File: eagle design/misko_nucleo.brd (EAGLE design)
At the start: 115 x 73 mm, 91 parts, among them CN1 LiPo Battery, IC1 TPS63031, IC1101 47309-2651, IC1201 FM25W256, IC1301 ADXL345, IC1302 74HCT1G32GW, IC2 RN4678_BT_MODULE, IC3 MAX6818, Q1 BSS84, Q1701 SQ2310ES-T1_BE3, Q1702 SQ2310ES-T1_BE3, Q1703 SQ2310ES-T1_BE3, SW1 MICROJOYSTICK, SW2 PB6156RSL, SW3 PB6156RSL, U1 SN74LVC1G3157DBVR - BT switch, U2 ATMEGA1281-16AU, U3 MCP73871-2AAI/ML, U4 SN74LVC1G3157DBVR - GPS switch, X1 FH12-30S-0.5SH

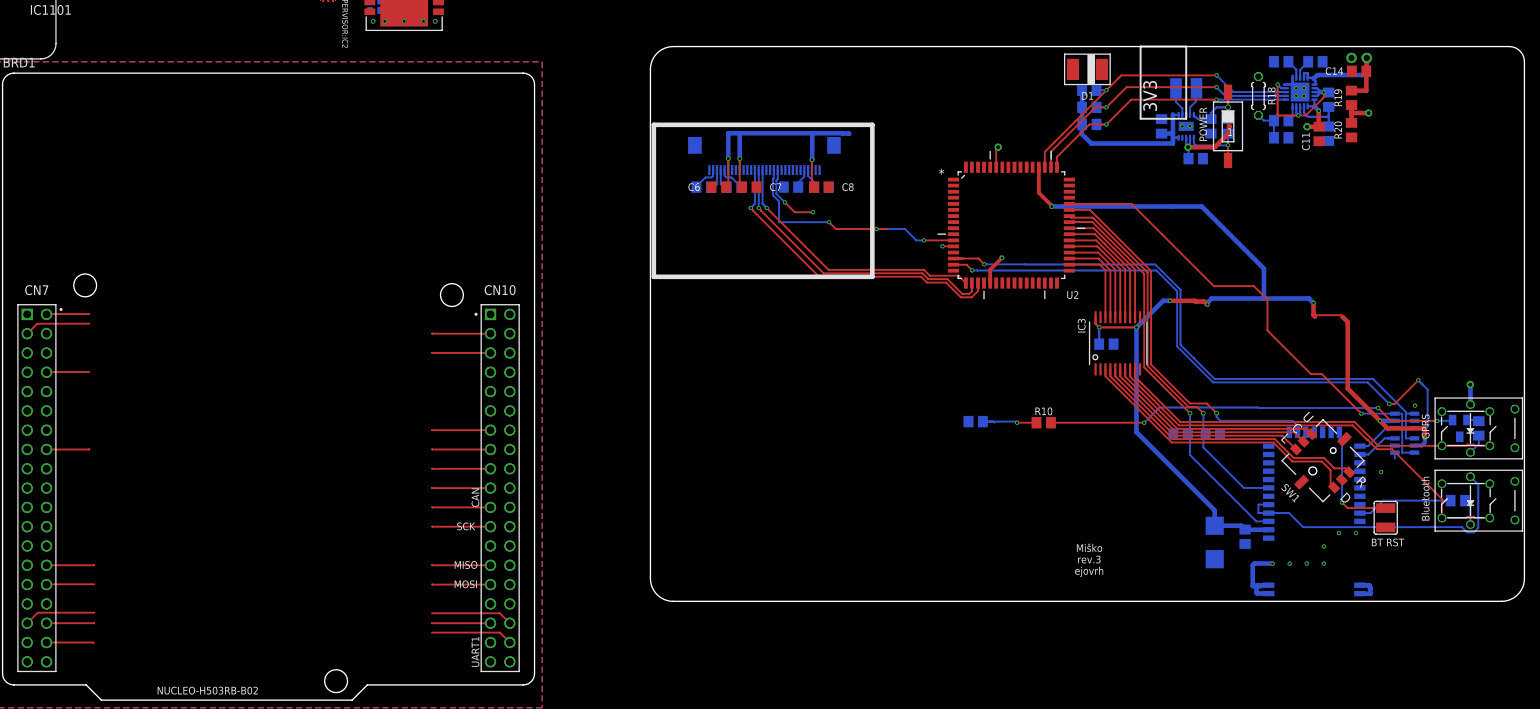
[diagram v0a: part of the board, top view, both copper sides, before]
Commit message: in misko.ioc: - moved SPI1_SD_CS from PA1 to PA2 - added timer2 rotary encoder GPIOs on PA1 and PB2 - added I2C2 in DMA mode
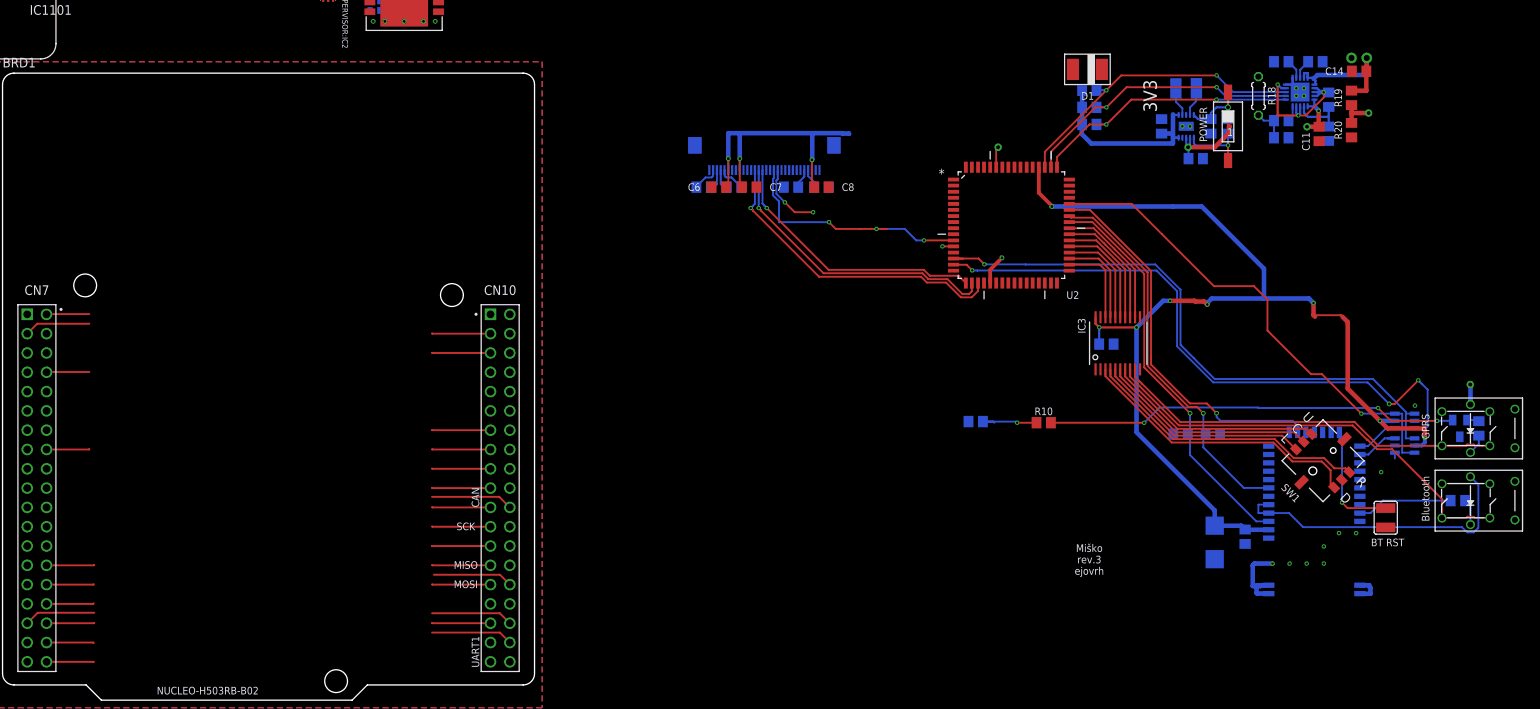
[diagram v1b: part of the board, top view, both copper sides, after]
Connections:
- net PB10 renamed I2C2_SCL
- net PB13 renamed I2C2_SDA
- net PB2 renamed ROTARY_CH1
- removed net PA2: BRD1.CN7_32
- new net ROTARY_CH2: BRD1.CN7_30
- net SPI1_SD_CS: now also BRD1.CN7_32; no longer BRD1.CN7_30
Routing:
- net ROTARY_CH1: track 0.00 -> 10.8 mm
- net I2C2_SDA: track 0.00 -> 10.5 mm
- net I2C2_SCL: track 0.00 -> 7.72 mm
- net ROTARY_CH2: track 0.00 -> 6.23 mm
- net LED_YELLOW: track 0.00 -> 6.23 mm
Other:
- board size 115 x 73 mm -> 70 x 82.5 mm
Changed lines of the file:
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@@
 <board>
 <plain>
-<wire x1="88.25" y1="13" x2="197.25" y2="13" width="0.1" layer="20"/>
-<wire x1="200.25" y1="16" x2="200.25" y2="84" width="0.1" layer="20"/>
-<wire x1="198.25" y1="86" x2="88.25" y2="86" width="0.1" layer="20"/>
-<wire x1="85.25" y1="83" x2="85.25" y2="16" width="0.1" layer="20"/>
-<wire x1="85.25" y1="83" x2="88.25" y2="86" width="0.1" layer="20" curve="-90"/>
-<wire x1="85.25" y1="16" x2="88.25" y2="13" width="0.1" layer="20" curve="90"/>
-<wire x1="197.25" y1="13" x2="200.25" y2="16" width="0.1" layer="20" curve="90"/>
-<wire x1="198.25" y1="86" x2="200.25" y2="84" width="0.1" layer="20" curve="-90"/>
-<wire x1="168" y1="78.25" x2="149.2" y2="78.15" width="0.5" layer="22" style="shortdash"/>
 <wire x1="156" y1="72.75" x2="154.5" y2="72.75" width="0.5" layer="22" style="shortdash"/>
-<wire x1="131" y1="72.75" x2="149.2" y2="72.65" width="0.5" layer="22" style="shortdash"/>
-<wire x1="149.2" y1="72.65" x2="149.2" y2="78.15" width="0.5" layer="22" style="shortdash"/>
-<wire x1="114.45" y1="55.7" x2="114.45" y2="75.7" width="0.6" layer="21"/>
-<wire x1="85.7" y1="55.7" x2="85.7" y2="75.7" width="0.6" layer="21"/>
-<wire x1="85.7" y1="55.7" x2="114.45" y2="55.7" width="0.6" layer="21"/>
-<wire x1="85.7" y1="75.7" x2="114.45" y2="75.7" width="0.6" layer="21"/>
 <text x="151" y="79.5" size="1.778" layer="21" font="vector" rot="R90" align="center">3V3</text>
 <text x="158" y="75.75" size="1" layer="21" font="vector" rot="R270" align="center">POWER</text>
@@
 <wire x1="179.75" y1="77.25" x2="168" y2="77.25" width="0.5" layer="22" style="shortdash"/>
 <text x="182.25" y="20.75" size="1" layer="21" font="vector" align="center">BT RST</text>
-<wire x1="171.75" y1="75.25" x2="171.75" y2="41.5" width="0.5" layer="22" style="shortdash"/>
-<wire x1="171.75" y1="41.5" x2="193.25" y2="41.5" width="0.5" layer="22" style="shortdash"/>
-<wire x1="149.75" y1="86" x2="155.75" y2="86" width="0.25" layer="21"/>
-<wire x1="155.75" y1="86" x2="155.75" y2="76.5" width="0.25" layer="21"/>
-<wire x1="155.75" y1="76.5" x2="149.75" y2="76.5" width="0.25" layer="21"/>
-<wire x1="149.75" y1="76.5" x2="149.75" y2="86" width="0.25" layer="21"/>
 <text x="143" y="16.5" size="1" layer="21" align="bottom-center">Miško
 rev.3
@@
 <contactref element="BRD1" pad="CN7_38"/>
 <contactref element="Q1703" pad="1"/>
-<wire x1="5.79" y1="5.04" x2="18.55" y2="-7.65" width="0" layer="19" extent="16-16"/>
+<wire x1="5.79" y1="5.04" x2="11.96" y2="5.04" width="0.25" layer="1"/>
+<wire x1="11.96" y1="5.04" x2="12" y2="5" width="0.25" layer="1"/>
+<wire x1="12" y1="5" x2="18.55" y2="-7.65" width="0" layer="19" extent="1-16"/>
 </signal>
 <signal name="PA15" class="2">
@@
 </signal>
 <signal name="SPI1_SD_CS" class="2">
-<contactref element="BRD1" pad="CN7_30"/>
-<wire x1="5.79" y1="15.2" x2="5.83" y2="15.24" width="0.25" layer="1"/>
-<wire x1="5.83" y1="15.24" x2="12.065" y2="15.24" width="0.25" layer="1"/>
 <contactref element="IC1101" pad="CD/DAT3"/>
-<wire x1="5.79" y1="15.2" x2="3.78" y2="97.74" width="0" layer="19" extent="1-1"/>
+<contactref element="BRD1" pad="CN7_32"/>
+<wire x1="5.79" y1="12.66" x2="11.91" y2="12.66" width="0.25" layer="1"/>
+<wire x1="11.91" y1="12.66" x2="12" y2="12.75" width="0.25" layer="1"/>
+<wire x1="5.79" y1="12.66" x2="3.78" y2="97.74" width="0" layer="19" extent="1-1"/>
 </signal>
 <signal name="ADC_VGPS" class="2">
@@
 <contactref element="BRD1" pad="CN10_24"/>
 </signal>
-<signal name="PB2" class="2">
+<signal name="ROTARY_CH1" class="2">
 <contactref element="BRD1" pad="CN10_22"/>
+<wire x1="66.75" y1="25.36" x2="65.36" y2="26.75" width="0.25" layer="1"/>
+<wire x1="65.36" y1="26.75" x2="56.5" y2="26.75" width="0.25" layer="1"/>
 </signal>
 <signal name="SPI1_MISO" class="2">
@@
 <wire x1="65.44" y1="8.89" x2="56.515" y2="8.89" width="0.25" layer="1"/>
 </signal>
-<signal name="PB10" class="2">
+<signal name="I2C2_SCL" class="2">
 <contactref element="BRD1" pad="CN10_25"/>
+<wire x1="64.21" y1="20.28" x2="56.53" y2="20.28" width="0.25" layer="1"/>
+<wire x1="56.53" y1="20.28" x2="56.5" y2="20.25" width="0.25" layer="1"/>
 </signal>
 <signal name="PN12" class="2">
 <contactref element="BRD1" pad="CN10_16"/>
 </signal>
-<signal name="PB13" class="2">
+<signal name="I2C2_SDA" class="2">
 <contactref element="BRD1" pad="CN10_30"/>
+<wire x1="66.75" y1="15.2" x2="65.45" y2="16.5" width="0.25" layer="1"/>
+<wire x1="65.45" y1="16.5" x2="56.75" y2="16.5" width="0.25" layer="1"/>
 </signal>
 <signal name="5V0" class="3">
@@
 <signal name="ADXL345:ADXL345_INT2">
 <contactref element="IC1301" pad="INT2"/>
-</signal>
-<signal name="PA2" class="2">
-<contactref element="BRD1" pad="CN7_32"/>
 </signal>
 <signal name="GPS:SUPERCAP+CHARGER:VMID" class="2">
@@
 <wire x1="5.79" y1="7.58" x2="-18.65" y2="77.2" width="0" layer="19" extent="16-16"/>
 </signal>
+<signal name="ROTARY_CH2" class="2">
+<contactref element="BRD1" pad="CN7_30"/>
+<wire x1="5.79" y1="15.2" x2="11.95" y2="15.2" width="0.25" layer="1"/>
+<wire x1="11.95" y1="15.2" x2="12" y2="15.25" width="0.25" layer="1"/>
+</signal>
 </signals>

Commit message: in sch & brd: - changed hierarchical module names so that board components have shorter names (GPS subsystem stuff) - added CAN infra. components to sch
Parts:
- removed C1, C10, C13, C8: 10µF, rcl:C0805
- removed C11, C14: 10µF, resistor:C0805
- removed C12: 1000µF, rcl:E5-10,5
- removed C2: 0.1µF, rcl:C0805
- removed C3, C4, C6, C7: 1µF, rcl:C0805
- removed C5: 22µF, rcl:C0805
- removed C9: 2.2µF / 25V, rcl:C0805
- removed CN1: LiPo Battery, SIM800C:JST-PH-2-THM-RA
- removed D1: BZG05C3V6-E3-TR3, zener:DO-214
- removed D2: SZ1SMB5916BT3G, diode:SMB
- removed D3: BAT60AE6327, diode:SOD323_ST
- removed GPS:ORG1510:IC1: ORG1510-MK4, ORG1510-MK4 GPS module:SMD
- removed GPS:SUPERCAP+CHARGER:C1, GPS:SUPERCAP+CHARGER:C34: 100u / 16V, rcl:C1210
- removed GPS:SUPERCAP+CHARGER:C24: 1.5F, EECS5R5H155 Supercap:TH
- removed GPS:SUPERCAP+CHARGER:C38, GPS:VOLTAGE_SUPERVISOR:C1, GPS:VOLTAGE_SUPERVISOR:C2: 0.1u / 16V, rcl:C0402
- removed GPS:SUPERCAP+CHARGER:IC2: LTC4425EDD#PBF, LTC4425 Supercap Charger:DFN-12
- removed GPS:SUPERCAP+CHARGER:R1: 33R, resistor:R1206
- removed GPS:SUPERCAP+CHARGER:R14: 10k, resistor:R0402
- removed GPS:SUPERCAP+CHARGER:R40, GPS:SUPERCAP+CHARGER:R41: 150k, resistor:R0402
- removed GPS:VOLTAGE_SUPERVISOR:IC2: TPS3808G33DBVT, TPS3808 - Supervisory Circuit:WSON-6
- removed GPS:VOLTAGE_SUPERVISOR:R18: 100k, resistor:R0402
- removed IC1: TPS63031, TPS63031 - Buck Boost Voltage Regulator:SMT
- removed IC2: RN4678_BT_MODULE, RN4678 Bluetooth 4.2 Dual Mode:SMT
- removed IC3: MAX6818, MAX6818 CMOS Switch debouncer:TSSOP20
- removed L1: DJNR3015-1R5, DJNR3015-1R5 Inductor:FFF
- removed Q1: BSS84, transistor-small-signal:SOT23
- removed R1, R10, R12, R13, R9: 10k, resistor:R0805
- removed R11, R6: 1k, resistor:R0805
- removed R14, R15: 1k, rcl:R0805
- removed R16, R2: 100k, rcl:R0805
- removed R17, R3: 270k, rcl:R0805
- removed R18: NTC 10k, rcl:0204/5
- removed R19, R20: 150k, rcl:R0805
- removed R4, R5, R7: 47k, rcl:R0805
- removed R8: 390k, rcl:R0805
- removed S1: POWER SWITCH, smd-special:SMS-001
- removed SJ1: RESET, jumper:SJW
- removed SW1: MICROJOYSTICK, micro joystick:MICROJOYSTICK
- removed SW2, SW3: PB6156RSL, PB6156RSL Illuminated Tact SPST-NO switch:TH
- removed U1: SN74LVC1G3157DBVR - BT switch, Texas Instruments_By_element14_Batch_1:SOT95P280X145-6N
- removed U2: ATMEGA1281-16AU, Atmel_By_element14_Batch_1-00:QFP80P1600X1600X120-64N
- removed U3: MCP73871-2AAI/ML, MCP73871 - Powerpath and Charge Controller:QFN50P400X400X100-21N
- removed U4: SN74LVC1G3157DBVR - GPS switch, Texas Instruments_By_element14_Batch_1:SOT95P280X145-6N
- removed X1: FH12-30S-0.5SH, con-hirose:FH12-30S-0.5SH
- added C401: 47nF / 10V, rcl:C0402
- added C405: 0.1uF / 10V, rcl:C0402
- added GPS:G:IC1: ORG1510-MK4, ORG1510-MK4 GPS module:SMD
- added GPS:SC:C1, GPS:SC:C34: 100u / 16V, rcl:C1210
- added GPS:SC:C24: 1.5F, EECS5R5H155 Supercap:TH
- added GPS:SC:C38, GPS:SV:C1, GPS:SV:C2: 0.1u / 16V, rcl:C0402
- added GPS:SC:IC2: LTC4425EDD#PBF, LTC4425 Supercap Charger:DFN-12
- added GPS:SC:R1: 33R, resistor:R1206
- added GPS:SC:R14: 10k, resistor:R0402
- added GPS:SC:R40, GPS:SC:R41: 150k, resistor:R0402
- added GPS:SV:IC2: TPS3808G33DBVT, TPS3808 - Supervisory Circuit:WSON-6
- added GPS:SV:R18: 100k, resistor:R0402
- added IC401: TCAN334, TCAN33x - 3.3V CAN Transciever:SOT23-8
- added J1: CAN, con-amp:10X02MTA
- added R401, R405: 60, rcl:R0805
- moved C1201 0.25 mm to (24.5, 96.5)
- moved IC1301 0.15 mm to (29.8, 96.5)
- moved C1131 0.15 mm to (0.25, 95.2)
- moved IC1302 0.11 mm to (29.5, 96.5)
- moved C1304 0.11 mm to (32.2, 95.2)
- moved IC1201 0.10 mm to (21.2, 96.5)
- moved IC1101 0.08 mm to (1.00, 99.0)
- renumbered GPS:ORG1510:C1 to GPS:G:C1, GPS:ORG1510:C2 to GPS:G:C2, GPS:ORG1510:C22 to GPS:G:C22, GPS:ORG1510:C31 to GPS:G:C31, GPS:ORG1510:R1 to GPS:G:R1, GPS:ORG1510:R2 to GPS:G:R2, GPS:SUPERCAP+CHARGER:Q4 to GPS:SC:Q4
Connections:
- removed net ADXL345_INT1_INTERRUPT_PIN: U2.25
- removed net ANALOG_SW_CTRL_PIN: U1.6, U2.44, U4.6
- removed net AREF: U2.62
- removed net AVCC: U2.64
- removed net BAT_A_PIN: R19.2, R20.1, U2.59
- removed net BLUETOOTH_PROF_IND_PIN: IC2.P0_5, U2.43
- removed net BLUETOOTH_RX: IC2.RXD, U1.4
- removed net BLUETOOTH_SWITCH_PIN: IC2.SW_BTN, R13.2, U2.41
- removed net BLUETOOTH_TX: IC2.TXD, U4.3
- removed net BLUETOOTH_WAKEUP_PIN: IC2.WAKEUP, R12.2, U2.42
- removed net BT_LED: IC2.LED, R6.1
- removed net BUTTON_BLUETOOTH: IC3.IN7, SW3.3, SW3.4
- removed net BUTTON_CENTER: IC3.IN5, SW1.CENTER
- removed net BUTTON_DOWN: IC3.IN2, SW1.DOWN
- removed net BUTTON_GPRS: IC3.IN8, SW2.3, SW2.4
- removed net BUTTON_LEFT: IC3.IN4, SW1.LEFT
- removed net BUTTON_RIGHT: IC3.IN3, SW1.RIGHT
- removed net BUTTON_UP: IC3.IN6, SW1.UP
- removed net CAP1N: C3.1, X1.5
- removed net CAP1P: C3.2, X1.4
- removed net CAP2N: C4.1, X1.3
- removed net CAP2P: C4.2, X1.2
- removed net EN: IC1.6_EN, R1.2, S1.1
- removed net GPRS_NETLIGHT: R10.1, R9.1
- removed net GPRS_NETLIGHT_GATE: Q1.1, R10.2
- removed net GPS:ORG1510:GPS_RX: GPS:G:C31.1, GPS:G:R2.2, GPS:ORG1510:IC1.RX_10
- removed net GPS:ORG1510:GPS_TX: GPS:G:C22.1, GPS:G:R1.2, GPS:ORG1510:IC1.3_TX
- removed net GPS:SUPERCAP+CHARGER:N$1: GPS:SC:Q4.3, GPS:SUPERCAP+CHARGER:R1.1
- removed net GPS:SUPERCAP+CHARGER:PFI: GPS:SUPERCAP+CHARGER:IC2.PFI, GPS:SUPERCAP+CHARGER:R40.1, GPS:SUPERCAP+CHARGER:R41.2
- removed net GPS:SUPERCAP+CHARGER:PFI_RET: GPS:SUPERCAP+CHARGER:IC2.PFI_RET, GPS:SUPERCAP+CHARGER:R41.1
- removed net GPS:SUPERCAP+CHARGER:PROG: GPS:SUPERCAP+CHARGER:IC2.PROG, GPS:SUPERCAP+CHARGER:R14.2
- removed net GPS:SUPERCAP+CHARGER:VMID: GPS:SUPERCAP+CHARGER:C1.1, GPS:SUPERCAP+CHARGER:C34.2, GPS:SUPERCAP+CHARGER:IC2.VMID
- removed net GPS:VOLTAGE_SUPERVISOR:CT: GPS:VOLTAGE_SUPERVISOR:IC2.CT
- removed net GPS:VOLTAGE_SUPERVISOR:SENSE: GPS:VOLTAGE_SUPERVISOR:C1.1, GPS:VOLTAGE_SUPERVISOR:IC2.SENSE
- removed net GPS_GREEN_LED_PIN: U2.48
- removed net GPS_POWER_CTL_PIN: U2.45
- removed net GPS_RED_LED_PIN: U2.47
- removed net GPS_SW_SERIAL_RX: U1.1, U2.14, U4.4
- removed net GPS_WAKEUP_PIN: U2.46
- removed net IREF: R8.2, X1.26
- removed net JTAG_TCL_PIN: U2.57
- removed net JTAG_TDI_PIN: U2.54
- removed net JTAG_TDO_PIN: U2.55
- removed net JTAG_TMS_PIN: U2.56
- removed net L2: R6.2, SW3.L2
- removed net LDO18_O: IC2.LDO18_O
- removed net LDO33_O: IC2.LDO33_O, IC2.VDD_IO, SW3.L1
- removed net L_L1: IC1.4_L1, L1.P$1
- removed net L_L2: IC1.2_L2, L1.P$2
- removed net MCP73871_CHARGE_STATUS_1_PIN: R7.2, U2.51, U3.8_STAT1
- removed net MCP73871_CHARGE_STATUS_2_PIN: R5.2, U2.50, U3.7_STAT2
- removed net MCP73871_POWER_GOOD_PIN: R4.2, U2.49, U3.!6_PG!
- removed net MENU_BLUETOOTH_POWER_BUTTON_PIN: IC3.OUT7, U2.39
- removed net MENU_CENTER_BUTTON_PIN: IC3.OUT5, U2.37
- removed net MENU_DOWN_BUTTON_PIN: IC3.OUT2, U2.34
- removed net MENU_GPRS_POWER_BUTTON_PIN: IC3.OUT8, U2.40
- removed net MENU_LEFT_BUTTON_PIN: IC3.OUT4, U2.36
- removed net MENU_RIGHT_BUTTON_PIN: IC3.OUT3, U2.35
- removed net MENU_UP_BUTTON_PIN: IC3.OUT6, U2.38
- removed net N$1: R11.1, SW2.L2
- removed net N$11: IC2.!RST_N!, SJ1.1
- removed net N$19: R14.2, R17.1, R18.1
- removed net N$3: Q1.2, R11.2
- removed net N$6: C12.+, D3.C
- removed net OLD_5V0: D3.A, R2.1, U3.17_CE, U3.18_IN1, U3.19_IN2, U3.3_SEL, U3.4_PROG2, U3.9_!TE!
- removed net PDI_UART0_CTS_PIN: U2.1
- removed net PDI_UART0_RX_PIN: U2.2
- removed net PDI_UART0_TX_PIN: U2.3
- removed net PN12: BRD1.CN10_16
- removed net PROG1: R15.1, U3.13_PROG1
- removed net PROG3: R16.1, U3.12_PROG3
- removed net RESET: U2.20
- removed net RTC_INT_INTERRUPT_PIN: U2.26
- removed net SD_CARD_DETECT_PIN: U2.4
- removed net SPI_MISO_PIN: U2.13
- removed net SPI_MOSI_PIN: U2.12, X1.19
- removed net SPI_OLED_D/C_PIN: U2.17, X1.15
- removed net SPI_OLED_RESET_PIN: U2.18, X1.14
- removed net SPI_SCK_PIN: U2.11, X1.18
- removed net SPI_SS_ADXL345_PIN: U2.16
- removed net SPI_SS_FRAM_PIN: U2.10
- removed net SPI_SS_OLED_PIN: U2.19, X1.13
- removed net SPI_SS_RTC_PIN: U2.7
- removed net SPI_SS_SD_CARD_PIN: U2.5
- removed net THERM: R14.1, U3.5_THERM
- removed net TMP36_VSENSE_PIN: U2.58
- removed net UART1_GPS_RX: U2.27
- removed net UART1_GPS_TX: U2.28
- removed net VCC: C10.1, C13.1, C5.2, C6.2, C7.2, C8.2, D1.CAT, D2.C, IC1.10_FB, IC1.1_VOUT, IC2.BAT_IN, IC3.VCC, R4.1, R5.1, R7.1, U1.5, U2.21, U2.52, U4.5, X1.28, X1.6, X1.9
- removed net VCC_SENSE_PIN: U2.60
- removed net VCOMH: C9.2, X1.27
- removed net VPCC: R2.2, R3.1, U3.2_VPCC
- removed net V_LIION+: C14.1, CN1.1, R19.1, U3.14_VBAT1, U3.15_VBAT2, U3.16_BAT_SENSE
- removed net V_LIION_REGULATED: C1.2, C11.1, C2.1, IC1.5_VIN, IC1.7_PS/SYNC, IC1.8_VINA, S1.2, SW2.L1, U3.1_OUT1, U3.20_OUT2
- removed net XTAL1: U2.24
- removed net XTAL2: U2.23
- new net CAN_!STBY!: BRD1.CN10_16, IC401.P$8
- new net CAN_H: IC401.P$7, J1.1, R401.2
- new net CAN_INFRA:SPLIT: C401.1, R401.1, R405.2
- new net CAN_L: IC401.P$6, J1.2, R405.1
- new net GPS:G:GPS_RX: GPS:G:C31.1, GPS:G:IC1.RX_10, GPS:G:R2.2
- new net GPS:G:GPS_TX: GPS:G:C22.1, GPS:G:IC1.3_TX, GPS:G:R1.2
- new net GPS:SC:N$1: GPS:SC:Q4.3, GPS:SC:R1.1
- new net GPS:SC:PFI: GPS:SC:IC2.PFI, GPS:SC:R40.1, GPS:SC:R41.2
- new net GPS:SC:PFI_RET: GPS:SC:IC2.PFI_RET, GPS:SC:R41.1
- new net GPS:SC:PROG: GPS:SC:IC2.PROG, GPS:SC:R14.2
- new net GPS:SC:VMID: GPS:SC:C1.1, GPS:SC:C34.2, GPS:SC:IC2.VMID
- new net GPS:SV:CT: GPS:SV:IC2.CT
- net 3V3: now also C405.1, GPS:SC:C38.1, GPS:SC:IC2.FB, GPS:SC:IC2.SEL, GPS:SC:IC2.VIN1, GPS:SC:IC2.VIN2, GPS:SC:R40.2, GPS:SV:C2.1, GPS:SV:IC2.VDD, GPS:SV:R18.2, IC401.P$3; no longer GPS:SUPERCAP+CHARGER:C38.1, GPS:SUPERCAP+CHARGER:IC2.FB, GPS:SUPERCAP+CHARGER:IC2.SEL, GPS:SUPERCAP+CHARGER:IC2.VIN1, GPS:SUPERCAP+CHARGER:IC2.VIN2, GPS:SUPERCAP+CHARGER:R40.2, GPS:VOLTAGE_SUPERVISOR:C2.1, GPS:VOLTAGE_SUPERVISOR:IC2.VDD, GPS:VOLTAGE_SUPERVISOR:R18.2
- net CAN_RX: now also IC401.P$4
- net CAN_TX: now also IC401.P$1
- net GND: now also C401.2, C405.2, GPS:G:IC1.5_GND, GPS:G:IC1.GND1, GPS:G:IC1.GND10, GPS:G:IC1.GND12, GPS:G:IC1.GND13, GPS:G:IC1.GND14, GPS:G:IC1.GND15, GPS:G:IC1.GND2, GPS:G:IC1.GND4, GPS:G:IC1.GND5, GPS:G:IC1.GND6, GPS:G:IC1.GND7, GPS:G:IC1.GND8, GPS:G:IC1.GND9, GPS:SC:C1.2, GPS:SC:C24.-, GPS:SC:C38.2, GPS:SC:IC2.GND, GPS:SC:R14.1, GPS:SV:C1.2, GPS:SV:C2.2, GPS:SV:IC2.GND1, GPS:SV:IC2.GND2, IC401.P$2; no longer C1.1, C10.2, C11.2, C12.-, C13.2, C14.2, C2.2, C5.1, C6.1, C7.1, C8.1, C9.1, CN1.2, D1.AN, D2.A, GPS:ORG1510:IC1.5_GND, GPS:ORG1510:IC1.GND1, GPS:ORG1510:IC1.GND10, GPS:ORG1510:IC1.GND12, GPS:ORG1510:IC1.GND13, GPS:ORG1510:IC1.GND14, GPS:ORG1510:IC1.GND15, GPS:ORG1510:IC1.GND2, GPS:ORG1510:IC1.GND4, GPS:ORG1510:IC1.GND5, GPS:ORG1510:IC1.GND6, GPS:ORG1510:IC1.GND7, GPS:ORG1510:IC1.GND8, GPS:ORG1510:IC1.GND9, GPS:SUPERCAP+CHARGER:C1.2, GPS:SUPERCAP+CHARGER:C24.-, GPS:SUPERCAP+CHARGER:C38.2, GPS:SUPERCAP+CHARGER:IC2.GND, GPS:SUPERCAP+CHARGER:R14.1, GPS:VOLTAGE_SUPERVISOR:C1.2, GPS:VOLTAGE_SUPERVISOR:C2.2, GPS:VOLTAGE_SUPERVISOR:IC2.GND1, GPS:VOLTAGE_SUPERVISOR:IC2.GND2, IC1.3_PGND, IC1.9_GND1, IC1.GND2, IC1.GND3, IC1.GND4, IC2.GND, IC2.GND1, IC2.GND10, IC2.GND11, IC2.GND12, IC2.GND2, IC2.GND3, IC2.GND4, IC2.GND5, IC2.GND6, IC2.GND7, IC2.GND8, IC2.GND9, IC3.!EN!, IC3.GND, Q1.3, R1.1, R12.1, R13.1, R15.2, R16.2, R17.2, R18.2, R20.2, R3.2, R8.1, R9.2, SJ1.2, SW1.GND1, SW1.GND2, SW1.GND3, SW2.1, SW2.2, SW2.GND1, SW2.GND2, SW3.1, SW3.2, SW3.GND1, SW3.GND2, U1.2, U2.22, U2.53, U2.63, U3.10_GND1, U3.11_GND2, U3.GND2, U3.GND3, U3.GND4, U3.GND5, U3.GND6, U4.2, X1.1, X1.10, X1.11, X1.12, X1.29, X1.30, X1.8
- net GPS:GPS_ON_OFF: now also GPS:G:IC1.1_ON_OFF, GPS:SV:IC2.!RESET!, GPS:SV:R18.1; no longer GPS:ORG1510:IC1.1_ON_OFF, GPS:VOLTAGE_SUPERVISOR:IC2.!RESET!, GPS:VOLTAGE_SUPERVISOR:R18.1
- net GPS:VGPS: now also GPS:G:IC1.4_VCC, GPS:SC:C24.+, GPS:SC:C34.1, GPS:SC:IC2.VOUT1, GPS:SC:IC2.VOUT2, GPS:SC:R1.2, GPS:SV:C1.1, GPS:SV:IC2.SENSE; no longer GPS:ORG1510:IC1.4_VCC, GPS:SUPERCAP+CHARGER:C24.+, GPS:SUPERCAP+CHARGER:C34.1, GPS:SUPERCAP+CHARGER:IC2.VOUT1, GPS:SUPERCAP+CHARGER:IC2.VOUT2, GPS:SUPERCAP+CHARGER:R1.2
- net GPS_!RESET!: now also GPS:G:IC1.!RESET!_8; no longer GPS:ORG1510:IC1.!RESET!_8
- net GPS_MCU_RX: no longer U1.3, U2.15
- net GPS_MCU_TX: no longer U4.1
- net GPS_PWR_CTRL: now also GPS:SV:IC2.!MR!; no longer GPS:VOLTAGE_SUPERVISOR:IC2.!MR!
- net GPS_WKUP: now also GPS:G:IC1.WAKEUP_6; no longer GPS:ORG1510:IC1.WAKEUP_6
- net SUPERCAP_!EN!: now also GPS:SC:IC2.EN; no longer GPS:SUPERCAP+CHARGER:IC2.EN
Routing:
- net VCC: track 219.0 -> 0.00 mm, vias 12 -> 0
- net GPS_MCU_RX: track 84.8 -> 0.00 mm, vias 3 -> 0
- net GPS_SW_SERIAL_RX: track 79.3 -> 0.00 mm, vias 1 -> 0
- net ANALOG_SW_CTRL_PIN: track 64.4 -> 0.00 mm, vias 1 -> 0
- net BUTTON_BLUETOOTH: track 57.6 -> 0.00 mm
- net GPRS_NETLIGHT_GATE: track 54.5 -> 0.00 mm, vias 3 -> 0
- net BLUETOOTH_SWITCH_PIN: track 53.3 -> 0.00 mm, vias 1 -> 0
- net BUTTON_GPRS: track 51.6 -> 0.00 mm
- net BLUETOOTH_WAKEUP_PIN: track 51.2 -> 0.00 mm, vias 1 -> 0
- net BLUETOOTH_PROF_IND_PIN: track 50.2 -> 0.00 mm, vias 1 -> 0
- net SPI_SS_OLED_PIN: track 41.4 -> 0.00 mm, vias 1 -> 0
- net MCP73871_CHARGE_STATUS_1_PIN: track 40.1 -> 0.00 mm, vias 2 -> 0
- net LDO33_O: track 39.8 -> 0.00 mm
- net SPI_OLED_RESET_PIN: track 39.0 -> 0.00 mm, vias 1 -> 0
- net MCP73871_CHARGE_STATUS_2_PIN: track 38.2 -> 0.00 mm, vias 2 -> 0
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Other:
- board text added: "H"
- board text added: "L"
- board text added: "info"
- board text removed: "3V3"
- board text removed: "BT RST"
- board text removed: "Bluetooth"
- board text removed: "GPRS"
- board text removed: "LiPo"
- board text removed: "Miško rev.3 ejovrh"
- board text removed: "POWER"
